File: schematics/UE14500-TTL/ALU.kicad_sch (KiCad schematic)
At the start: 9 parts, among them U12 74LS86, U13 74LS00, U14 74LS151, U2 74LS08, U9 74LS02

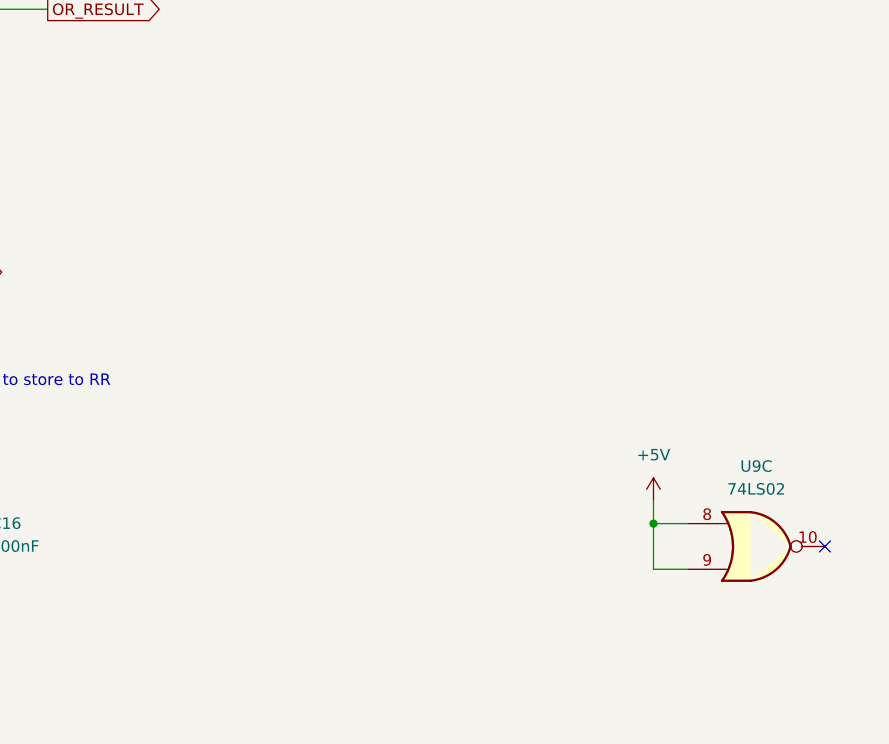
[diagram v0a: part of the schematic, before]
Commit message: Add a tape "REWIND" opcode to reset the PC early
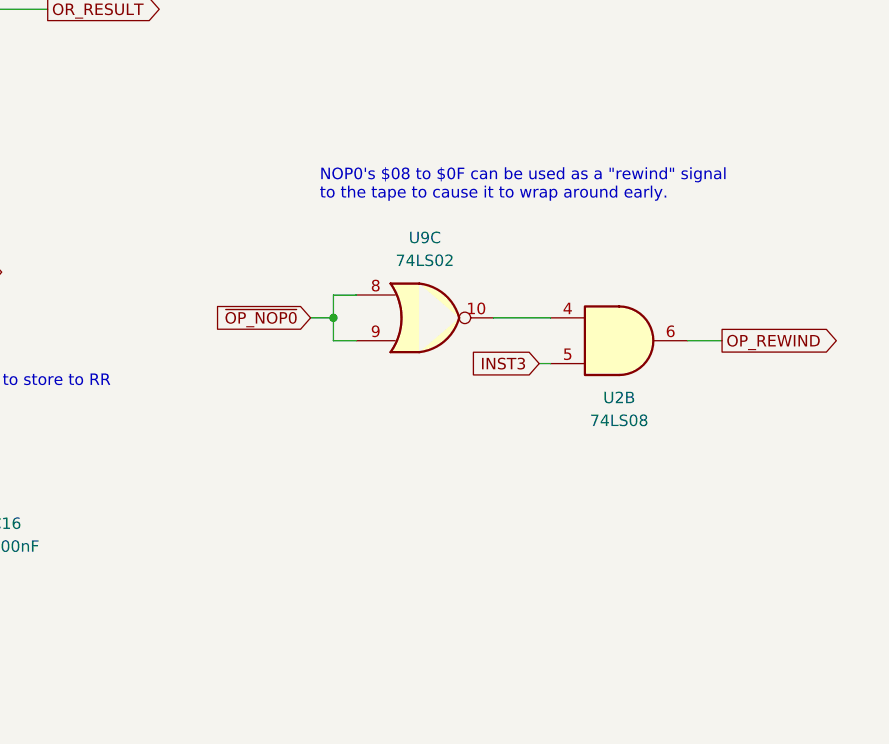
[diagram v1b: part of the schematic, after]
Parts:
- added unit 2 of U2
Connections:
- net +5V: no longer U9.8, U9.9
- net at U9.10: now also U2.4
- new net INST3: U2.5
- new net OP_REWIND: U2.6
- new net ~{OP_NOP0}: U9.8, U9.9
- no-connect marks 2 -> 1
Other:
- note added: "NOP0's $08 to $0F can be used as a "rewind" signal to the tape to cause it to wrap around early."
- moved on the sheet: U9C
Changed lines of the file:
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@@
 	)
 	(junction
-		(at 251.46 147.32)
-		(diameter 0)
-		(color 0 0 0 0)
-	)
-	(junction
 		(at 115.57 57.15)
 		(diameter 0)
@@
 	)
 	(junction
+		(at 215.9 124.46)
+		(diameter 0)
+		(color 0 0 0 0)
+	)
+	(junction
 		(at 157.48 74.93)
 		(diameter 0)
@@
 	)
 	(no_connect
-		(at 270.51 149.86)
-	)
-	(no_connect
 		(at 162.56 121.92)
 	)
@@
 	(wire
 		(pts
-			(xy 251.46 144.78) (xy 251.46 147.32)
+			(xy 138.43 44.45) (xy 140.97 44.45)
 		)
 		(stroke
@@
 	(wire
 		(pts
-			(xy 138.43 44.45) (xy 140.97 44.45)
+			(xy 118.11 92.71) (xy 115.57 92.71)
 		)
 		(stroke
@@
 	(wire
 		(pts
-			(xy 118.11 92.71) (xy 115.57 92.71)
+			(xy 215.9 121.92) (xy 215.9 124.46)
 		)
 		(stroke
@@
 	(wire
 		(pts
+			(xy 255.27 127) (xy 259.08 127)
+		)
+		(stroke
+			(width 0)
+			(type default)
+		)
+	)
+	(wire
+		(pts
+			(xy 218.44 121.92) (xy 215.9 121.92)
+		)
+		(stroke
+			(width 0)
+			(type default)
+		)
+	)
+	(wire
+		(pts
 			(xy 118.11 72.39) (xy 113.03 72.39)
 		)
@@
 	(wire
 		(pts
+			(xy 215.9 127) (xy 218.44 127)
+		)
+		(stroke
+			(width 0)
+			(type default)
+		)
+	)
+	(wire
+		(pts
 			(xy 214.63 67.31) (xy 220.98 67.31)
 		)
@@
 	(wire
 		(pts
-			(xy 251.46 152.4) (xy 255.27 152.4)
+			(xy 213.36 124.46) (xy 215.9 124.46)
 		)
 		(stroke
@@
 	(wire
 		(pts
+			(xy 238.76 129.54) (xy 240.03 129.54)
+		)
+		(stroke
+			(width 0)
+			(type default)
+		)
+	)
+	(wire
+		(pts
 			(xy 107.95 41.91) (xy 113.03 41.91)
 		)
@@
 	(wire
 		(pts
-			(xy 251.46 147.32) (xy 255.27 147.32)
+			(xy 233.68 124.46) (xy 240.03 124.46)
 		)
 		(stroke
@@
 	(wire
 		(pts
+			(xy 215.9 124.46) (xy 215.9 127)
+		)
+		(stroke
+			(width 0)
+			(type default)
+		)
+	)
+	(wire
+		(pts
 			(xy 134.62 152.4) (xy 137.16 152.4)
 		)
@@
 	(wire
 		(pts
-			(xy 251.46 147.32) (xy 251.46 152.4)
-		)
-		(stroke
-			(width 0)
-			(type default)
-		)
-	)
-	(wire
-		(pts
 			(xy 69.85 71.12) (xy 69.85 73.66)
 		)
@@
 		)
 	)
+	(text "NOP0's $08 to $0F can be used as a \"rewind\" signal\nto the tape to cause it to wrap around early."
+		(exclude_from_sim no)
+		(at 214.376 109.728 0)
+		(effects
+			(font
+				(size 1.27 1.27)
+			)
+			(justify left)
+		)
+	)
 	(global_label "~{OP_SUB}"
 		(shape input)
@@
 		)
 	)
+	(global_label "OP_REWIND"
+		(shape output)
+		(at 259.08 127 0)
+		(fields_autoplaced yes)
+		(effects
+			(font
+				(size 1.27 1.27)
+			)
+			(justify left)
+		)
+		(property "Intersheetrefs" "${INTERSHEET_REFS}"
+			(at 272.709 127 0)
+			(effects
+				(font
+					(size 1.27 1.27)
+				)
+				(justify left)
+				(hide yes)
+			)
+		)
+	)
+	(global_label "~{OP_NOP0}"
+		(shape input)
+		(at 213.36 124.46 180)
+		(fields_autoplaced yes)
+		(effects
+			(font
+				(size 1.27 1.27)
+			)
+			(justify right)
+		)
+		(property "Intersheetrefs" "${INTERSHEET_REFS}"
+			(at 201.6662 124.46 0)
+			(effects
+				(font
+					(size 1.27 1.27)
+				)
+				(justify right)
+				(hide yes)
+			)
+		)
+	)
 	(global_label "CAR_VAL"
 		(shape output)
@@
 		)
 	)
+	(global_label "INST3"
+		(shape input)
+		(at 238.76 129.54 180)
+		(fields_autoplaced yes)
+		(effects
+			(font
+				(size 1.27 1.27)
+			)
+			(justify right)
+		)
+		(property "Intersheetrefs" "${INTERSHEET_REFS}"
+			(at 230.4529 129.54 0)
+			(effects
+				(font
+					(size 1.27 1.27)
+				)
+				(justify right)
+				(hide yes)
+			)
+		)
+	)
 	(global_label "NAND_RESULT"
 		(shape output)
@@
 	)
 	(symbol
-		(lib_id "power:+5V")
-		(at 251.46 144.78 0)
-		(unit 1)
-		(exclude_from_sim no)
-		(in_bom yes)
-		(on_board yes)
-		(dnp no)
-		(fields_autoplaced yes)
-		(property "Reference" "#PWR84"
-			(at 251.46 148.59 0)
-			(effects
-				(font
-					(size 1.27 1.27)
-				)
-				(hide yes)
-			)
-		)
-		(property "Value" "+5V"
-			(at 251.46 139.7 0)
-			(effects
-				(font
-					(size 1.27 1.27)
-				)
-			)
-		)
-		(property "Footprint" ""
-			(at 251.46 144.78 0)
-			(effects
-				(font
-					(size 1.27 1.27)
-				)
-				(hide yes)
-			)
-		)
-		(property "Datasheet" ""
-			(at 251.46 144.78 0)
-			(effects
-				(font
-					(size 1.27 1.27)
-				)
-				(hide yes)
-			)
-		)
-		(property "Description" "Power symbol creates a global label with name \"+5V\""
-			(at 251.46 144.78 0)
-			(effects
-				(font
-					(size 1.27 1.27)
-				)
-				(hide yes)
-			)
-		)
-		(pin "1"
-		)
-		(instances
-			(project "UE1-TTL-Tubeless"
-				(path "/3387ba40-0694-43b2-a156-d12ce9552f1f/4abc98b8-59b0-47a5-b354-2023193d4bfb"
-					(reference "#PWR84")
-					(unit 1)
-				)
-			)
-		)
-	)
-	(symbol
 		(lib_id "74xx:74LS00")
 		(at 170.18 64.77 0)
@@
 	)
 	(symbol
+		(lib_id "74xx:74LS08")
+		(at 247.65 127 0)
+		(unit 2)
+		(exclude_from_sim no)
+		(in_bom yes)
+		(on_board yes)
+		(dnp no)
+		(property "Reference" "U2"
+			(at 247.65 133.35 0)
+			(effects
+				(font
+					(size 1.27 1.27)
+				)
+			)
+		)
+		(property "Value" "74LS08"
+			(at 247.65 135.89 0)
+			(effects
+				(font
+					(size 1.27 1.27)
+				)
+			)
+		)
+		(property "Footprint" "Package_DIP:DIP-14_W7.62mm"
+			(at 247.65 127 0)
+			(effects
+				(font
+					(size 1.27 1.27)
+				)
+				(hide yes)
+			)
+		)
+		(property "Datasheet" "http://www.ti.com/lit/gpn/sn74LS08"
+			(at 247.65 127 0)
+			(effects
+				(font
+					(size 1.27 1.27)
+				)
+				(hide yes)
+			)
+		)
+		(property "Description" "Quad And2"
+			(at 247.65 127 0)
+			(effects
+				(font
+					(size 1.27 1.27)
+				)
+				(hide yes)
+			)
+		)
+		(pin "7"
+		)
+		(pin "8"
+		)
+		(pin "5"
+		)
+		(pin "9"
+		)
+		(pin "10"
+		)
+		(pin "1"
+		)
+		(pin "3"
+		)
+		(pin "14"
+		)
+		(pin "2"
+		)
+		(pin "6"
+		)
+		(pin "11"
+		)
+		(pin "4"
+		)
+		(pin "12"
+		)
+		(pin "13"
+		)
+		(instances
+			(project "UE14500-TTL"
+				(path "/3387ba40-0694-43b2-a156-d12ce9552f1f/4abc98b8-59b0-47a5-b354-2023193d4bfb"
+					(reference "U2")
+					(unit 2)
+				)
+			)
+		)
+	)
+	(symbol
 		(lib_id "power:GND")
 		(at 58.42 144.78 0)
@@
 	(symbol
 		(lib_id "74xx:74LS02")
-		(at 262.89 149.86 0)
+		(at 226.06 124.46 0)
 		(unit 3)
 		(exclude_from_sim no)
@@
 		(fields_autoplaced yes)
 		(property "Reference" "U9"
-			(at 262.89 140.97 0)
+			(at 226.06 115.57 0)
 			(effects
 				(font
@@
 		)
 		(property "Value" "74LS02"
-			(at 262.89 143.51 0)
+			(at 226.06 118.11 0)
 			(effects
 				(font
@@
 		)
 		(property "Footprint" "Package_DIP:DIP-14_W7.62mm"
-			(at 262.89 149.86 0)
+			(at 226.06 124.46 0)
 			(effects
 				(font
@@
 		)
 		(property "Datasheet" "http://www.ti.com/lit/gpn/sn74ls02"
-			(at 262.89 149.86 0)
+			(at 226.06 124.46 0)
 			(effects
 				(font
@@
 		)
 		(property "Description" "quad 2-input NOR gate"
-			(at 262.89 149.86 0)
+			(at 226.06 124.46 0)
 			(effects
 				(font

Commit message: Make some renderings of the computer
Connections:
- net OP_REWIND renamed REWIND
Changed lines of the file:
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@@
 		)
 	)
-	(global_label "OP_REWIND"
+	(global_label "REWIND"
 		(shape output)
 		(at 259.08 127 0)
@@
 		)
 		(property "Intersheetrefs" "${INTERSHEET_REFS}"
-			(at 272.709 127 0)
+			(at 269.1409 127 0)
 			(effects
 				(font
@@
 		(dnp no)
 		(fields_autoplaced yes)
-		(property "Reference" "#PWR82"
+		(property "Reference" "#PWR79"
 			(at 173.99 148.59 0)
 			(effects
@@
 			(project "UE14500-TTL"
 				(path "/3387ba40-0694-43b2-a156-d12ce9552f1f/4abc98b8-59b0-47a5-b354-2023193d4bfb"
-					(reference "#PWR82")
+					(reference "#PWR79")
 					(unit 1)
 				)
@@
 		(dnp no)
 		(fields_autoplaced yes)
-		(property "Reference" "#PWR81"
+		(property "Reference" "#PWR78"
 			(at 149.86 166.37 0)
 			(effects
@@
 			(project ""
 				(path "/3387ba40-0694-43b2-a156-d12ce9552f1f/4abc98b8-59b0-47a5-b354-2023193d4bfb"
-					(reference "#PWR81")
+					(reference "#PWR78")
 					(unit 1)
 				)
@@
 		(dnp no)
 		(fields_autoplaced yes)
-		(property "Reference" "#PWR70"
+		(property "Reference" "#PWR67"
 			(at 58.42 151.13 0)
 			(effects
@@
 			(project "UE14500-TTL"
 				(path "/3387ba40-0694-43b2-a156-d12ce9552f1f/4abc98b8-59b0-47a5-b354-2023193d4bfb"
-					(reference "#PWR70")
+					(reference "#PWR67")
 					(unit 1)
 				)
@@
 		(dnp no)
 		(fields_autoplaced yes)
-		(property "Reference" "#PWR80"
+		(property "Reference" "#PWR77"
 			(at 149.86 115.57 0)
 			(effects
@@
 			(project ""
 				(path "/3387ba40-0694-43b2-a156-d12ce9552f1f/4abc98b8-59b0-47a5-b354-2023193d4bfb"
-					(reference "#PWR80")
+					(reference "#PWR77")
 					(unit 1)
 				)
@@
 		(dnp no)
 		(fields_autoplaced yes)
-		(property "Reference" "#PWR78"
+		(property "Reference" "#PWR75"
 			(at 134.62 129.54 0)
 			(effects
@@
 			(project "UE1-TTL-Tubeless"
 				(path "/3387ba40-0694-43b2-a156-d12ce9552f1f/4abc98b8-59b0-47a5-b354-2023193d4bfb"
-					(reference "#PWR78")
+					(reference "#PWR75")
 					(unit 1)
 				)
@@
 		(dnp no)
 		(fields_autoplaced yes)
-		(property "Reference" "#PWR72"
+		(property "Reference" "#PWR69"
 			(at 58.42 191.77 0)
 			(effects
@@
 			(project "UE1-TTL-Tubeless"
 				(path "/3387ba40-0694-43b2-a156-d12ce9552f1f/4abc98b8-59b0-47a5-b354-2023193d4bfb"
-					(reference "#PWR72")
+					(reference "#PWR69")
 					(unit 1)
 				)
@@
 		(dnp no)
 		(fields_autoplaced yes)
-		(property "Reference" "#PWR67"
+		(property "Reference" "#PWR64"
 			(at 34.29 163.83 0)
 			(effects
@@
 			(project "UE1-TTL-Tubeless"
 				(path "/3387ba40-0694-43b2-a156-d12ce9552f1f/4abc98b8-59b0-47a5-b354-2023193d4bfb"
-					(reference "#PWR67")
+					(reference "#PWR64")
 					(unit 1)
 				)
@@
 		(dnp no)
 		(fields_autoplaced yes)
-		(property "Reference" "#PWR69"
+		(property "Reference" "#PWR66"
 			(at 58.42 140.97 0)
 			(effects
@@
 			(project "UE14500-TTL"
 				(path "/3387ba40-0694-43b2-a156-d12ce9552f1f/4abc98b8-59b0-47a5-b354-2023193d4bfb"
-					(reference "#PWR69")
+					(reference "#PWR66")
 					(unit 1)
 				)
@@
 		(dnp no)
 		(fields_autoplaced yes)
-		(property "Reference" "#PWR83"
+		(property "Reference" "#PWR80"
 			(at 173.99 158.75 0)
 			(effects
@@
 			(project "UE14500-TTL"
 				(path "/3387ba40-0694-43b2-a156-d12ce9552f1f/4abc98b8-59b0-47a5-b354-2023193d4bfb"
-					(reference "#PWR83")
+					(reference "#PWR80")
 					(unit 1)
 				)
@@
 		(dnp no)
 		(fields_autoplaced yes)
-		(property "Reference" "#PWR77"
+		(property "Reference" "#PWR74"
 			(at 113.03 128.27 0)
 			(effects
@@
 			(project "UE1-TTL-Tubeless"
 				(path "/3387ba40-0694-43b2-a156-d12ce9552f1f/4abc98b8-59b0-47a5-b354-2023193d4bfb"
-					(reference "#PWR77")
+					(reference "#PWR74")
 					(unit 1)
 				)
@@
 		(dnp no)
 		(fields_autoplaced yes)
-		(property "Reference" "#PWR68"
+		(property "Reference" "#PWR65"
 			(at 34.29 191.77 0)
 			(effects
@@
 			(project "UE1-TTL-Tubeless"
 				(path "/3387ba40-0694-43b2-a156-d12ce9552f1f/4abc98b8-59b0-47a5-b354-2023193d4bfb"
-					(reference "#PWR68")
+					(reference "#PWR65")
 					(unit 1)
 				)
@@
 		(dnp no)
 		(fields_autoplaced yes)
-		(property "Reference" "#PWR65"
+		(property "Reference" "#PWR62"
 			(at 34.29 140.97 0)
 			(effects
@@
 			(project "UE14500-TTL"
 				(path "/3387ba40-0694-43b2-a156-d12ce9552f1f/4abc98b8-59b0-47a5-b354-2023193d4bfb"
-					(reference "#PWR65")
+					(reference "#PWR62")
 					(unit 1)
 				)
@@
 		(dnp no)
 		(fields_autoplaced yes)
-		(property "Reference" "#PWR66"
+		(property "Reference" "#PWR63"
 			(at 34.29 151.13 0)
 			(effects
@@
 			(project "UE14500-TTL"
 				(path "/3387ba40-0694-43b2-a156-d12ce9552f1f/4abc98b8-59b0-47a5-b354-2023193d4bfb"
-					(reference "#PWR66")
+					(reference "#PWR63")
 					(unit 1)
 				)
@@
 		(dnp no)
 		(fields_autoplaced yes)
-		(property "Reference" "#PWR75"
+		(property "Reference" "#PWR72"
 			(at 81.28 163.83 0)
 			(effects
@@
 			(project "UE1-TTL-Tubeless"
 				(path "/3387ba40-0694-43b2-a156-d12ce9552f1f/4abc98b8-59b0-47a5-b354-2023193d4bfb"
-					(reference "#PWR75")
+					(reference "#PWR72")
 					(unit 1)
 				)
@@
 		(dnp no)
 		(fields_autoplaced yes)
-		(property "Reference" "#PWR76"
+		(property "Reference" "#PWR73"
 			(at 81.28 191.77 0)
 			(effects
@@
 			(project "UE1-TTL-Tubeless"
 				(path "/3387ba40-0694-43b2-a156-d12ce9552f1f/4abc98b8-59b0-47a5-b354-2023193d4bfb"
-					(reference "#PWR76")
+					(reference "#PWR73")
 					(unit 1)
 				)
@@
 		(dnp no)
 		(fields_autoplaced yes)
-		(property "Reference" "#PWR74"
+		(property "Reference" "#PWR71"
 			(at 81.28 151.13 0)
 			(effects
@@
 			(project "UE14500-TTL"
 				(path "/3387ba40-0694-43b2-a156-d12ce9552f1f/4abc98b8-59b0-47a5-b354-2023193d4bfb"
-					(reference "#PWR74")
+					(reference "#PWR71")
 					(unit 1)
 				)
@@
 		(dnp no)
 		(fields_autoplaced yes)
-		(property "Reference" "#PWR71"
+		(property "Reference" "#PWR68"
 			(at 58.42 163.83 0)
 			(effects
@@
 			(project "UE1-TTL-Tubeless"
 				(path "/3387ba40-0694-43b2-a156-d12ce9552f1f/4abc98b8-59b0-47a5-b354-2023193d4bfb"
-					(reference "#PWR71")
+					(reference "#PWR68")
 					(unit 1)
 				)
@@
 		(dnp no)
 		(fields_autoplaced yes)
-		(property "Reference" "#PWR73"
+		(property "Reference" "#PWR70"
 			(at 81.28 140.97 0)
 			(effects
@@
 			(project "UE14500-TTL"
 				(path "/3387ba40-0694-43b2-a156-d12ce9552f1f/4abc98b8-59b0-47a5-b354-2023193d4bfb"
-					(reference "#PWR73")
+					(reference "#PWR70")
 					(unit 1)
 				)
@@
 		(dnp no)
 		(fields_autoplaced yes)
-		(property "Reference" "#PWR79"
+		(property "Reference" "#PWR76"
 			(at 134.62 166.37 0)
 			(effects
@@
 			(project "UE1-TTL-Tubeless"
 				(path "/3387ba40-0694-43b2-a156-d12ce9552f1f/4abc98b8-59b0-47a5-b354-2023193d4bfb"
-					(reference "#PWR79")
+					(reference "#PWR76")
 					(unit 1)
 				)

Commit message: Lay out CPU board
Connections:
- net ~{OP_NOP0}: no longer U9.9
- net CAR_VAL renamed CAR_ALU
- net INST3 renamed MEM3
- net RR_VAL renamed RR_ALU
- new net SKIP: U9.9
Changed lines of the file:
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@@
-	)
-	(junction
-		(at 215.9 124.46)
-		(diameter 0)
-		(color 0 0 0 0)
 	)
 	(junction
@@
 	(wire
 		(pts
+			(xy 213.36 127) (xy 218.44 127)
+		)
+		(stroke
+			(width 0)
+			(type default)
+		)
+	)
+	(wire
+		(pts
 			(xy 60.96 110.49) (xy 68.58 110.49)
 		)
@@
 	(wire
 		(pts
-			(xy 215.9 121.92) (xy 215.9 124.46)
-		)
-		(stroke
-			(width 0)
-			(type default)
-		)
-	)
-	(wire
-		(pts
 			(xy 138.43 49.53) (xy 142.24 49.53)
 		)
@@
 	(wire
 		(pts
-			(xy 218.44 121.92) (xy 215.9 121.92)
-		)
-		(stroke
-			(width 0)
-			(type default)
-		)
-	)
-	(wire
-		(pts
 			(xy 118.11 72.39) (xy 113.03 72.39)
 		)
@@
 	(wire
 		(pts
-			(xy 215.9 127) (xy 218.44 127)
+			(xy 213.36 121.92) (xy 218.44 121.92)
 		)
 		(stroke
@@
 	(wire
 		(pts
-			(xy 213.36 124.46) (xy 215.9 124.46)
-		)
-		(stroke
-			(width 0)
-			(type default)
-		)
-	)
-	(wire
-		(pts
 			(xy 130.81 132.08) (xy 137.16 132.08)
 		)
@@
 		(pts
 			(xy 130.81 134.62) (xy 137.16 134.62)
-		)
-		(stroke
-			(width 0)
-			(type default)
-		)
-	)
-	(wire
-		(pts
-			(xy 215.9 124.46) (xy 215.9 127)
 		)
 		(stroke
@@
 		)
 	)
+	(global_label "SKIP"
+		(shape input)
+		(at 213.36 127 180)
+		(fields_autoplaced yes)
+		(effects
+			(font
+				(size 1.27 1.27)
+			)
+			(justify right)
+		)
+		(property "Intersheetrefs" "${INTERSHEET_REFS}"
+			(at 206.0205 127 0)
+			(effects
+				(font
+					(size 1.27 1.27)
+				)
+				(justify right)
+				(hide yes)
+			)
+		)
+	)
 	(global_label "RR"
 		(shape input)
@@
 		)
 	)
-	(global_label "RR_VAL"
+	(global_label "RR_ALU"
 		(shape output)
 		(at 170.18 119.38 0)
@@
 		)
 		(property "Intersheetrefs" "${INTERSHEET_REFS}"
-			(at 179.8781 119.38 0)
+			(at 180.12 119.38 0)
 			(effects
 				(font
@@
 	(global_label "~{OP_NOP0}"
 		(shape input)
-		(at 213.36 124.46 180)
-		(fields_autoplaced yes)
-		(effects
-			(font
-				(size 1.27 1.27)
-			)
-			(justify right)
-		)
-		(property "Intersheetrefs" "${INTERSHEET_REFS}"
-			(at 201.6662 124.46 0)
-			(effects
-				(font
-					(size 1.27 1.27)
-				)
-				(justify right)
-				(hide yes)
-			)
-		)
-	)
-	(global_label "CAR_VAL"
+		(at 213.36 121.92 180)
+		(fields_autoplaced yes)
+		(effects
+			(font
+				(size 1.27 1.27)
+			)
+			(justify right)
+		)
+		(property "Intersheetrefs" "${INTERSHEET_REFS}"
+			(at 201.6662 121.92 0)
+			(effects
+				(font
+					(size 1.27 1.27)
+				)
+				(justify right)
+				(hide yes)
+			)
+		)
+	)
+	(global_label "CAR_ALU"
 		(shape output)
 		(at 220.98 67.31 0)
@@
 		)
 		(property "Intersheetrefs" "${INTERSHEET_REFS}"
-			(at 231.7667 67.31 0)
+			(at 232.0086 67.31 0)
 			(effects
 				(font
@@
 		)
 	)
-	(global_label "INST3"
+	(global_label "MEM3"
 		(shape input)
 		(at 238.76 129.54 180)
@@
 		)
 		(property "Intersheetrefs" "${INTERSHEET_REFS}"
-			(at 230.4529 129.54 0)
-			(effects
-				(font
+			(at 230.5135 129.54 0)
+			(effects
+				(font

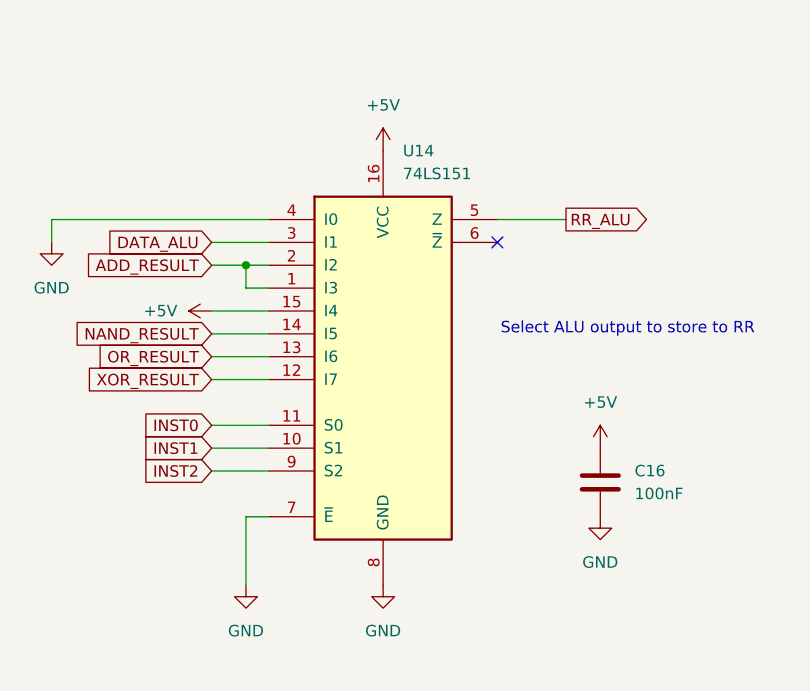
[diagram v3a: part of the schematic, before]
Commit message: Change 74LS151 to 74LS251
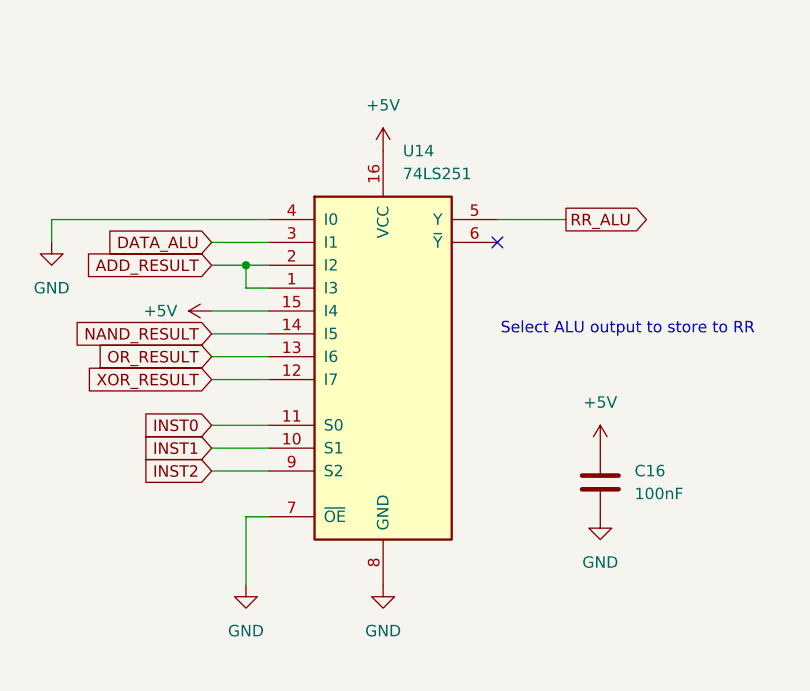
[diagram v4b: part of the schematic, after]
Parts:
- U14: value 74LS151 -> 74LS251; symbol 74xx:74LS151 -> 74xx:74LS251
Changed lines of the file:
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@@
 	)
 	(symbol
-		(lib_id "74xx:74LS151")
+		(lib_id "74xx:74LS251")
 		(at 149.86 134.62 0)
 		(unit 1)
@@
 			)
 		)
-		(property "Value" "74LS151"
+		(property "Value" "74LS251"
 			(at 152.0541 114.3 0)
 			(effects
@@
 			)
 		)
-		(property "Datasheet" "http://www.ti.com/lit/gpn/sn74LS151"
+		(property "Datasheet" "http://www.ti.com/lit/gpn/sn74LS251"
 			(at 149.86 134.62 0)
 			(effects
@@
 			)
 		)
-		(property "Description" "Multiplexer 8 to 1"
+		(property "Description" "Multiplexer 8 to 1, 3-state Outputs"
 			(at 149.86 134.62 0)
 			(effects
